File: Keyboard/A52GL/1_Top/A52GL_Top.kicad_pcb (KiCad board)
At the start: 2 copper layers, 315.8 x 99.2 mm, 68 parts, among them J10 Conn_01x01, J11 Conn_01x01, J12 Conn_01x01, J13 Conn_01x01, J14 Conn_01x01, J15 Conn_01x01, J16 Conn_01x01, J17 Conn_01x01, J2 Conn_01x01, J3 Conn_01x01, J4 Conn_01x01, J5 Conn_01x01, J6 Conn_01x01, J7 Conn_01x01, J8 Conn_01x01, J9 Conn_01x01, SW10 SW_PUSH, SW12 SW_PUSH, SW13 SW_PUSH, SW14 SW_PUSH, SW15 SW_PUSH, SW16 SW_PUSH, SW18 SW_PUSH, SW19 SW_PUSH, SW2 KEY_SWITCH, SW20 SW_PUSH, SW21 SW_PUSH, SW22 SW_PUSH, SW23 SW_PUSH, SW24 SW_PUSH, SW25 SW_PUSH, SW27 SW_PUSH, SW28 SW_PUSH, SW29 SW_PUSH, SW30 SW_PUSH, SW32 SW_PUSH, SW38 SW_PUSH, SW39 SW_PUSH, SW4 SW_PUSH, SW46 SW_PUSH, SW47 SW_PUSH, SW48 SW_PUSH, SW49 SW_PUSH, SW5 SW_PUSH, SW51 SW_PUSH, SW52 SW_PUSH, SW53 SW_PUSH, SW54 SW_PUSH, SW56 SW_PUSH, SW57 SW_PUSH, SW58 SW_PUSH, SW59 SW_PUSH, SW6 SW_PUSH, SW61 SW_PUSH, SW62 SW_PUSH, SW63 SW_PUSH, SW64 SW_PUSH, SW7 SW_PUSH, SW8 SW_PUSH

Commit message: 寸法更新とか
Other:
- board size 315.8 x 99.2 mm -> 314.4 x 98.8 mm
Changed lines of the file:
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@@
   (general
     (thickness 1.6)
-    (drawings 44)
+    (drawings 46)
     (tracks 0)
     (zones 0)
@@
     (fp_line (start 9.525 9.525) (end 9.525 -9.525) (layer F.Fab) (width 0.15))
   )
+  (gr_line (start 13.575 19.55) (end 13.575 113.75) (layer F.Fab) (width 0.15))
+  (gr_line (start 329.325 113.75) (end 329.325 19.55) (layer F.Fab) (width 0.15))
   (gr_line (start 10.075 122.75) (end 8.575 121.25) (layer F.Fab) (width 0.15))
   (gr_line (start 334.325 12.05) (end 332.825 10.55) (layer F.Fab) (width 0.15))
@@
   (gr_line (start 78.575 20.55) (end 264.325 20.55) (layer F.Fab) (width 0.15))
   (gr_line (start 10.45 50.55) (end 332.4 50.55) (layer F.Fab) (width 0.15))
-  (gr_arc (start 321.325 20.05) (end 324.325 20.05) (angle -90) (layer F.Fab) (width 0.1))
-  (gr_arc (start 321.325 113.25) (end 321.325 116.25) (angle -90) (layer F.Fab) (width 0.1))
-  (gr_arc (start 21.575 20.05) (end 21.575 17.05) (angle -90) (layer F.Fab) (width 0.1))
-  (gr_arc (start 21.575 113.25) (end 18.575 113.25) (angle -90) (layer F.Fab) (width 0.1))
+  (gr_arc (start 320.625 20.25) (end 323.625 20.25) (angle -90) (layer F.Fab) (width 0.1))
+  (gr_arc (start 320.625 113.05) (end 320.625 116.05) (angle -90) (layer F.Fab) (width 0.1))
+  (gr_arc (start 22.275 20.25) (end 22.275 17.25) (angle -90) (layer F.Fab) (width 0.1))
+  (gr_arc (start 22.275 113.05) (end 19.275 113.05) (angle -90) (layer F.Fab) (width 0.1))
   (gr_text "Do not place switches to the left of this line." (at 32.5 13.7) (layer F.Fab)
     (effects (font (size 1 1) (thickness 0.15)))
@@
     (effects (font (size 1 1) (thickness 0.15)))
   )
-  (gr_line (start 324.325 20.05) (end 324.325 113.25) (layer F.Fab) (width 0.1))
-  (gr_line (start 18.575 20.05) (end 18.575 113.25) (layer F.Fab) (width 0.1))
-  (gr_arc (start 16.575 113.25) (end 13.575 113.25) (angle -90) (layer Edge.Cuts) (width 0.1))
-  (gr_arc (start 16.575 20.05) (end 16.575 17.05) (angle -90) (layer Edge.Cuts) (width 0.1))
-  (gr_arc (start 326.325 20.05) (end 329.325 20.05) (angle -90) (layer Edge.Cuts) (width 0.1))
-  (gr_arc (start 326.325 113.25) (end 326.325 116.25) (angle -90) (layer Edge.Cuts) (width 0.1))
-  (gr_line (start 329.325 113.25) (end 329.325 20.05) (layer Edge.Cuts) (width 0.1))
-  (gr_line (start 16.575 116.25) (end 326.325 116.25) (layer Edge.Cuts) (width 0.1))
-  (gr_line (start 13.575 20.05) (end 13.575 113.25) (layer Edge.Cuts) (width 0.1))
-  (gr_line (start 326.325 17.05) (end 16.575 17.05) (layer Edge.Cuts) (width 0.1))
+  (gr_line (start 323.625 20.25) (end 323.625 113.05) (layer F.Fab) (width 0.1))
+  (gr_line (start 19.275 20.25) (end 19.275 113.05) (layer F.Fab) (width 0.1))
+  (gr_arc (start 17.275 113.05) (end 14.275 113.05) (angle -90) (layer Edge.Cuts) (width 0.1))
+  (gr_arc (start 17.275 20.25) (end 17.275 17.25) (angle -90) (layer Edge.Cuts) (width 0.1))
+  (gr_arc (start 325.625 20.25) (end 328.625 20.25) (angle -90) (layer Edge.Cuts) (width 0.1))
+  (gr_arc (start 325.625 113.05) (end 325.625 116.05) (angle -90) (layer Edge.Cuts) (width 0.1))
+  (gr_line (start 328.625 113.05) (end 328.625 20.25) (layer Edge.Cuts) (width 0.1))
+  (gr_line (start 17.275 116.05) (end 325.625 116.05) (layer Edge.Cuts) (width 0.1))
+  (gr_line (start 14.275 20.25) (end 14.275 113.05) (layer Edge.Cuts) (width 0.1))
+  (gr_line (start 325.625 17.25) (end 17.275 17.25) (layer Edge.Cuts) (width 0.1))
 )

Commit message: スイッチ穴の寸法を14.1mmに変更
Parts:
- SW10, SW12, SW13, SW14, SW15, SW16 (x2), SW18, SW19, SW20 (x2), SW21, SW22, SW23, SW24, SW25, SW27, SW28, SW29, SW30, SW32, SW38, SW39, SW4 (x2), SW46, SW47, SW48, SW51 (x2), SW52, SW53 (x3), SW54, SW56, SW57, SW58, SW59, SW63, SW64, SW7, SW8: footprint kbd_SW_Hole:SW_Hole -> kbd_SW_Hole:SW_Hole_1

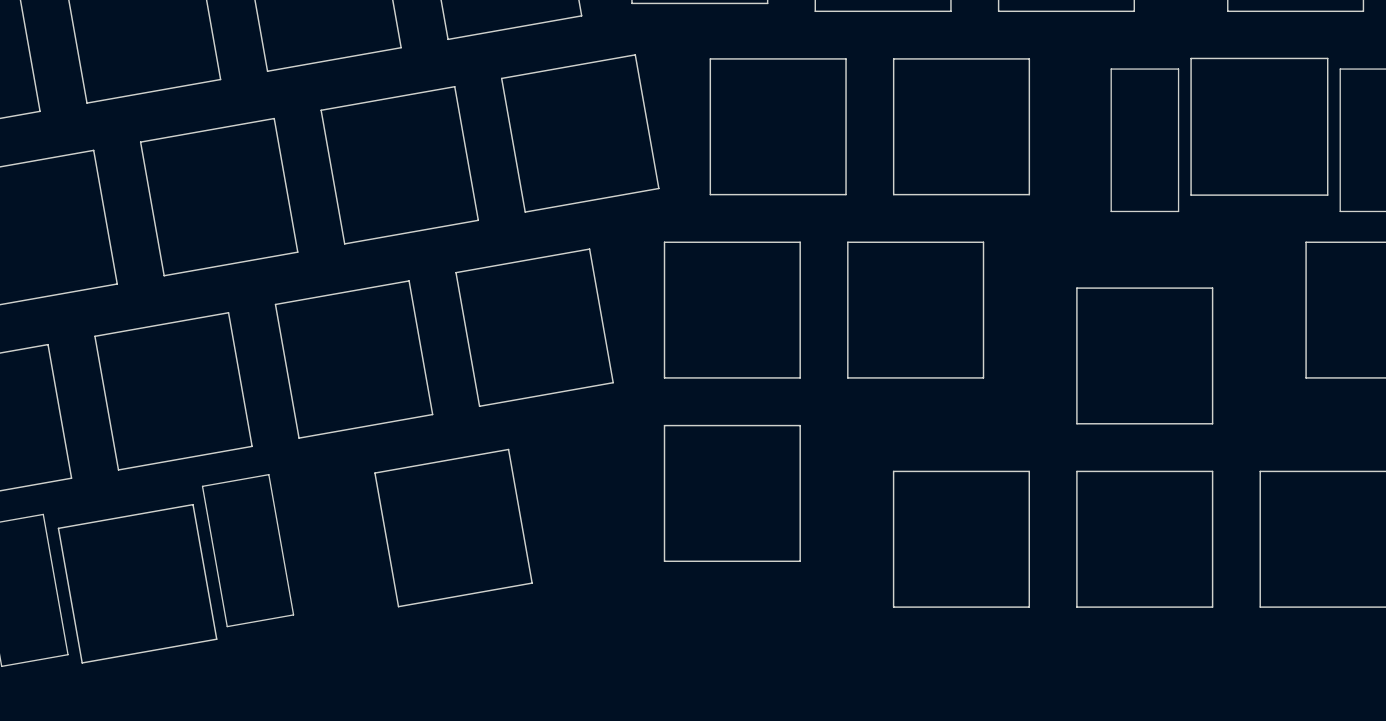
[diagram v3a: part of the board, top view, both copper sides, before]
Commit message: フットプリント名の変更に対応
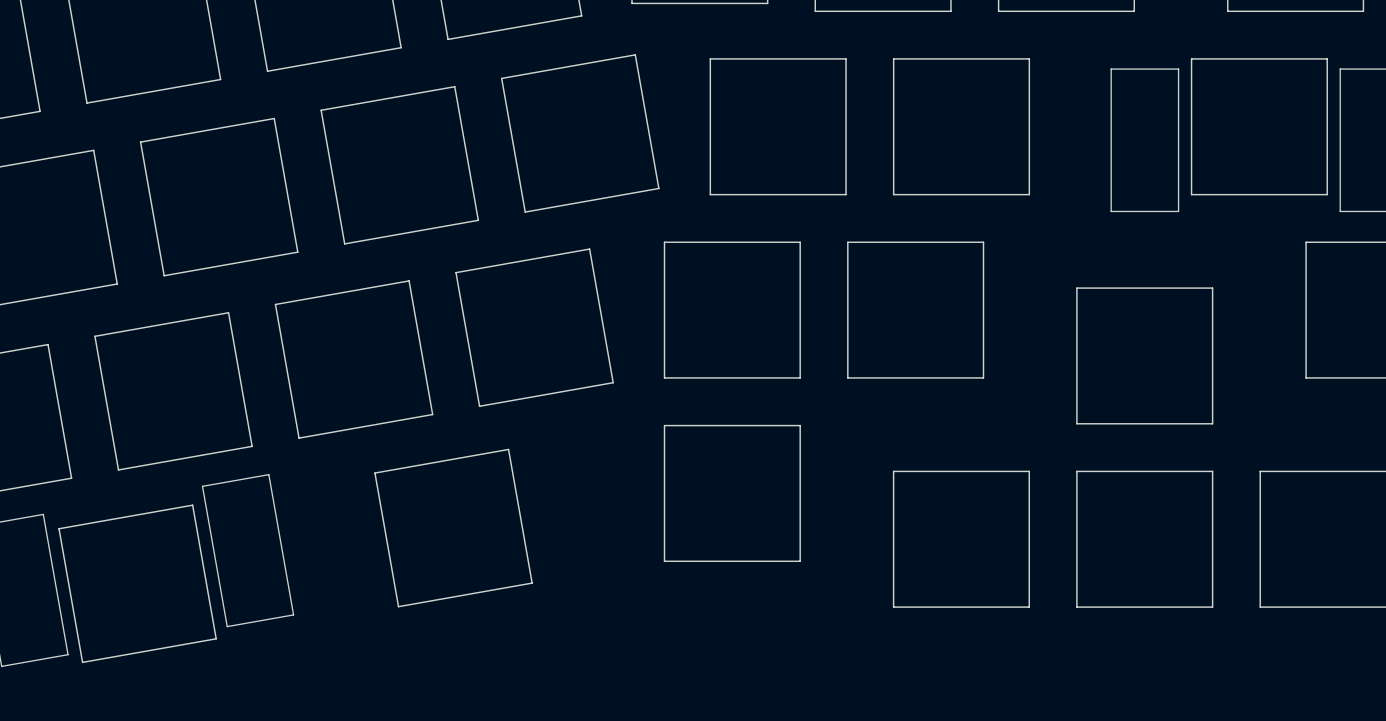
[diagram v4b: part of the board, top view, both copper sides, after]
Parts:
- SW10, SW12, SW13, SW14, SW15, SW16 (x2), SW18, SW19, SW20 (x2), SW21, SW22, SW23, SW24, SW25, SW27, SW28, SW29, SW30, SW32, SW38, SW39, SW4 (x2), SW46, SW47, SW48, SW51 (x2), SW52, SW53 (x3), SW54, SW56, SW57, SW58, SW59, SW63, SW64, SW7, SW8: footprint kbd_SW_Hole:SW_Hole_1 -> kbd_SW_Hole:SW_Hole_1u
- SW2: footprint kbd_SW_Hole:SW_Hole_2 -> kbd_SW_Hole:SW_Hole_2u
- SW23, SW62: footprint kbd_SW_Hole:SW_Hole_2.25 -> kbd_SW_Hole:SW_Hole_2.25u
- SW49, SW5, SW7 (x2): footprint kbd_SW_Hole:SW_Hole_1.25 -> kbd_SW_Hole:SW_Hole_1.25u
- SW6: footprint kbd_SW_Hole:SW_Hole_1.75 -> kbd_SW_Hole:SW_Hole_1.75u
